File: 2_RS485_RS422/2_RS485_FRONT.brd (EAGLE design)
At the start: 71.5 x 24 mm, 3 parts

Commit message: Cleanup, front with lib elements
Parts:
- removed E$1: (no value), AllSerialv2:PANEL
- removed E$2: (no value), AllSerialv2:RIA_AKL182-10
- removed E$3: (no value), AllSerialv2:LSTB-05-2
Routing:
- removed copper zone on layer 16, net S$1
- removed copper zone on layer 16, net S$2
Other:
- outline, holes or cut-outs redrawn
- board text added: "AllSerial RS485/422"
- board text removed: "AllSerial RS485/422 v1.1 46/18"
- board text removed: "RS485/422"

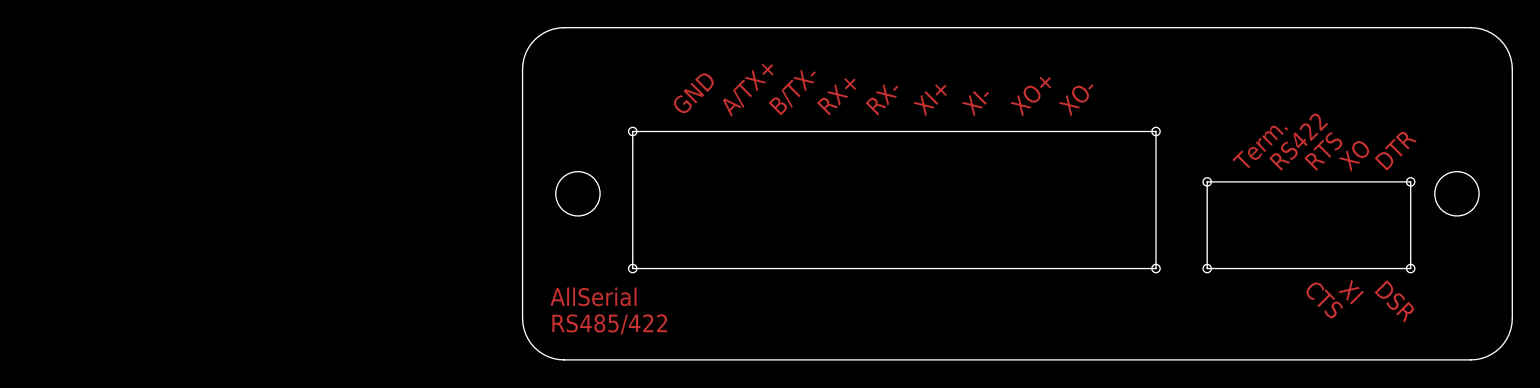
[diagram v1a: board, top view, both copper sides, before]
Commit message: pro mini layout corrected
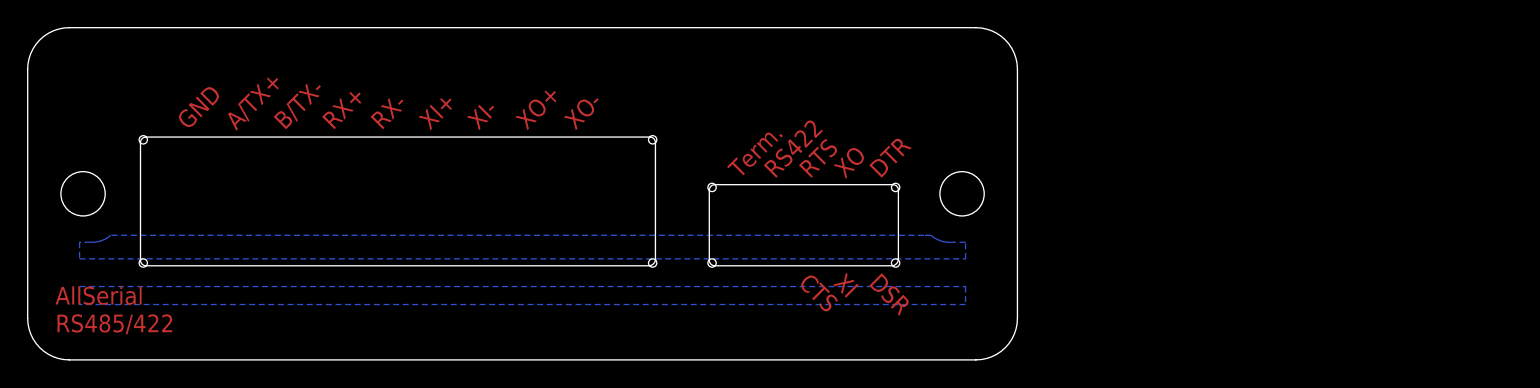
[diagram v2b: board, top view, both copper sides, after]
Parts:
- added E$1: (no value), AllSerialv2:PANEL
- added E$2: (no value), AllSerialv2:RIA_AKL182-10
- added E$3: (no value), AllSerialv2:LSTB-05-2
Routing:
- added copper zone on layer 16, net S$1
- added copper zone on layer 16, net S$2
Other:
- outline, holes or cut-outs redrawn
- board text added: "AllSerial RS485/422 v1.1 46/18"
- board text added: "RS485/422"
- board text removed: "AllSerial RS485/422"
